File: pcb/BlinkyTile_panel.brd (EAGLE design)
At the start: 220.1 x 170 mm, 220 parts

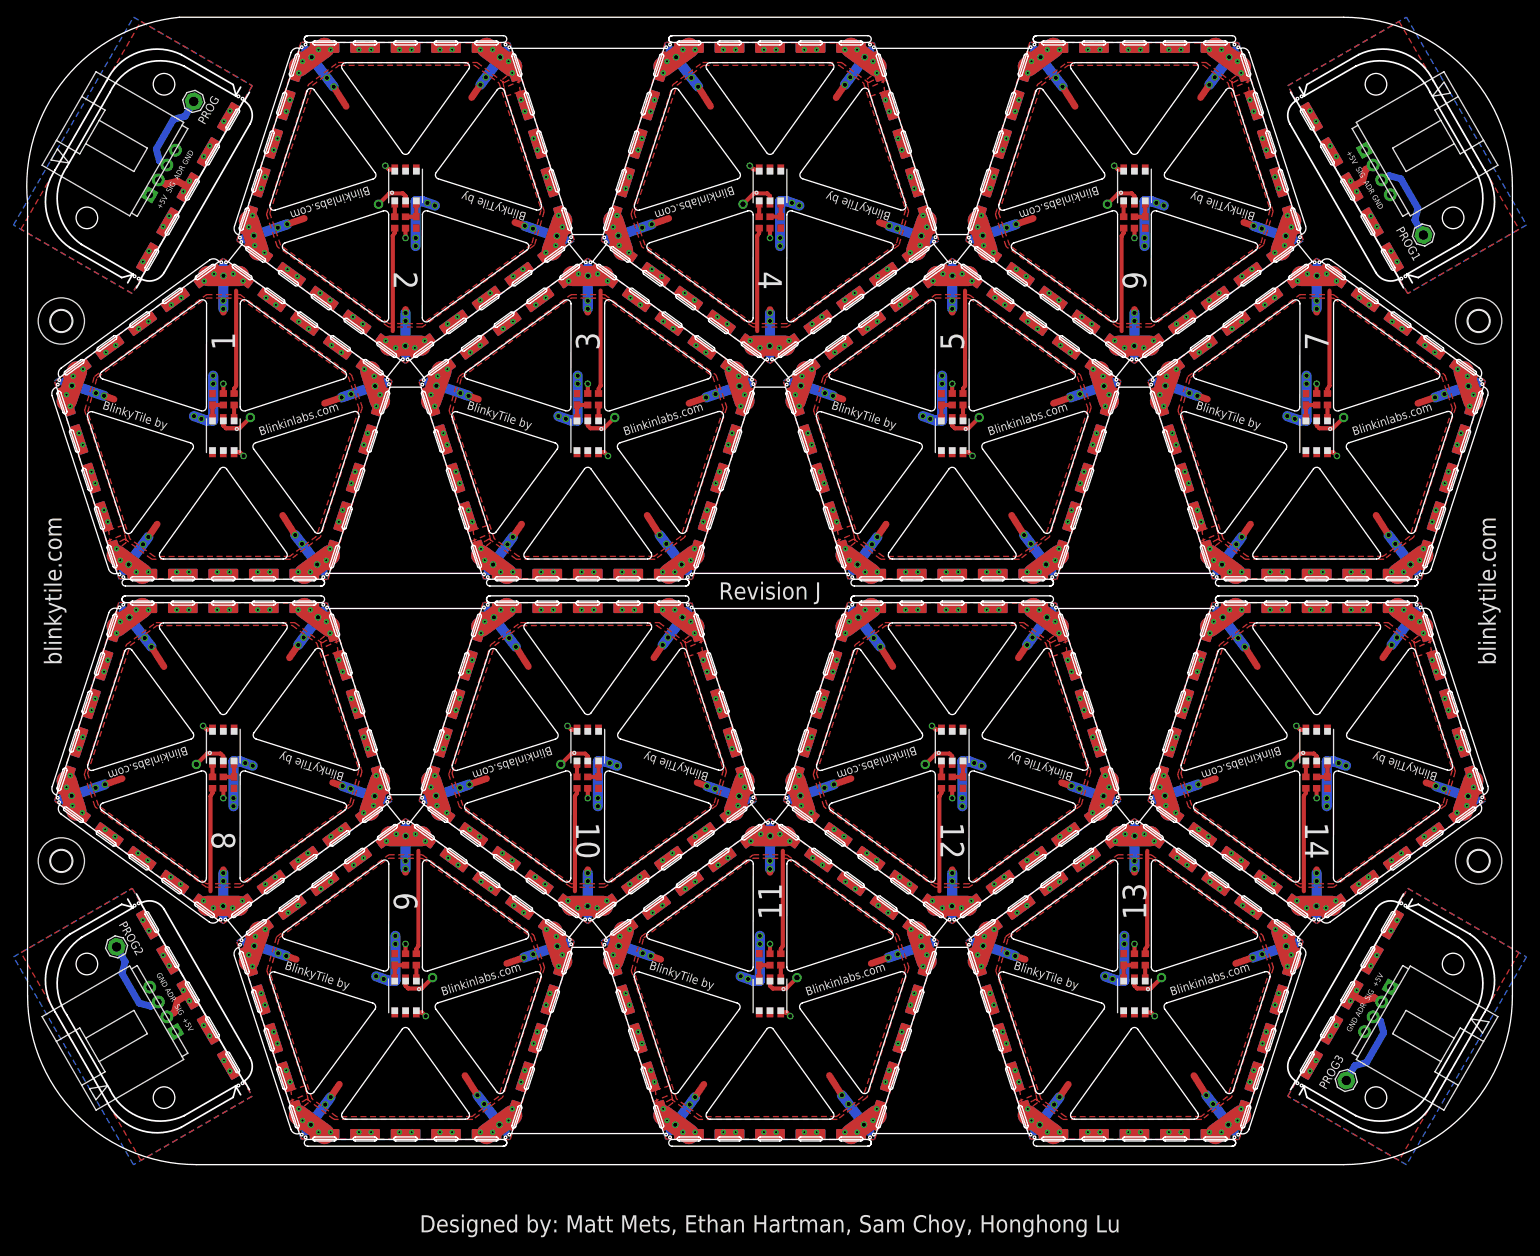
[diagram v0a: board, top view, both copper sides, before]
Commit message: Update panel
- fixed connector board error
- added  fiducial marker at corner
- removed mounting holes at side
- removed 2 connector boards on panel
- added remark for blinkyTile signal
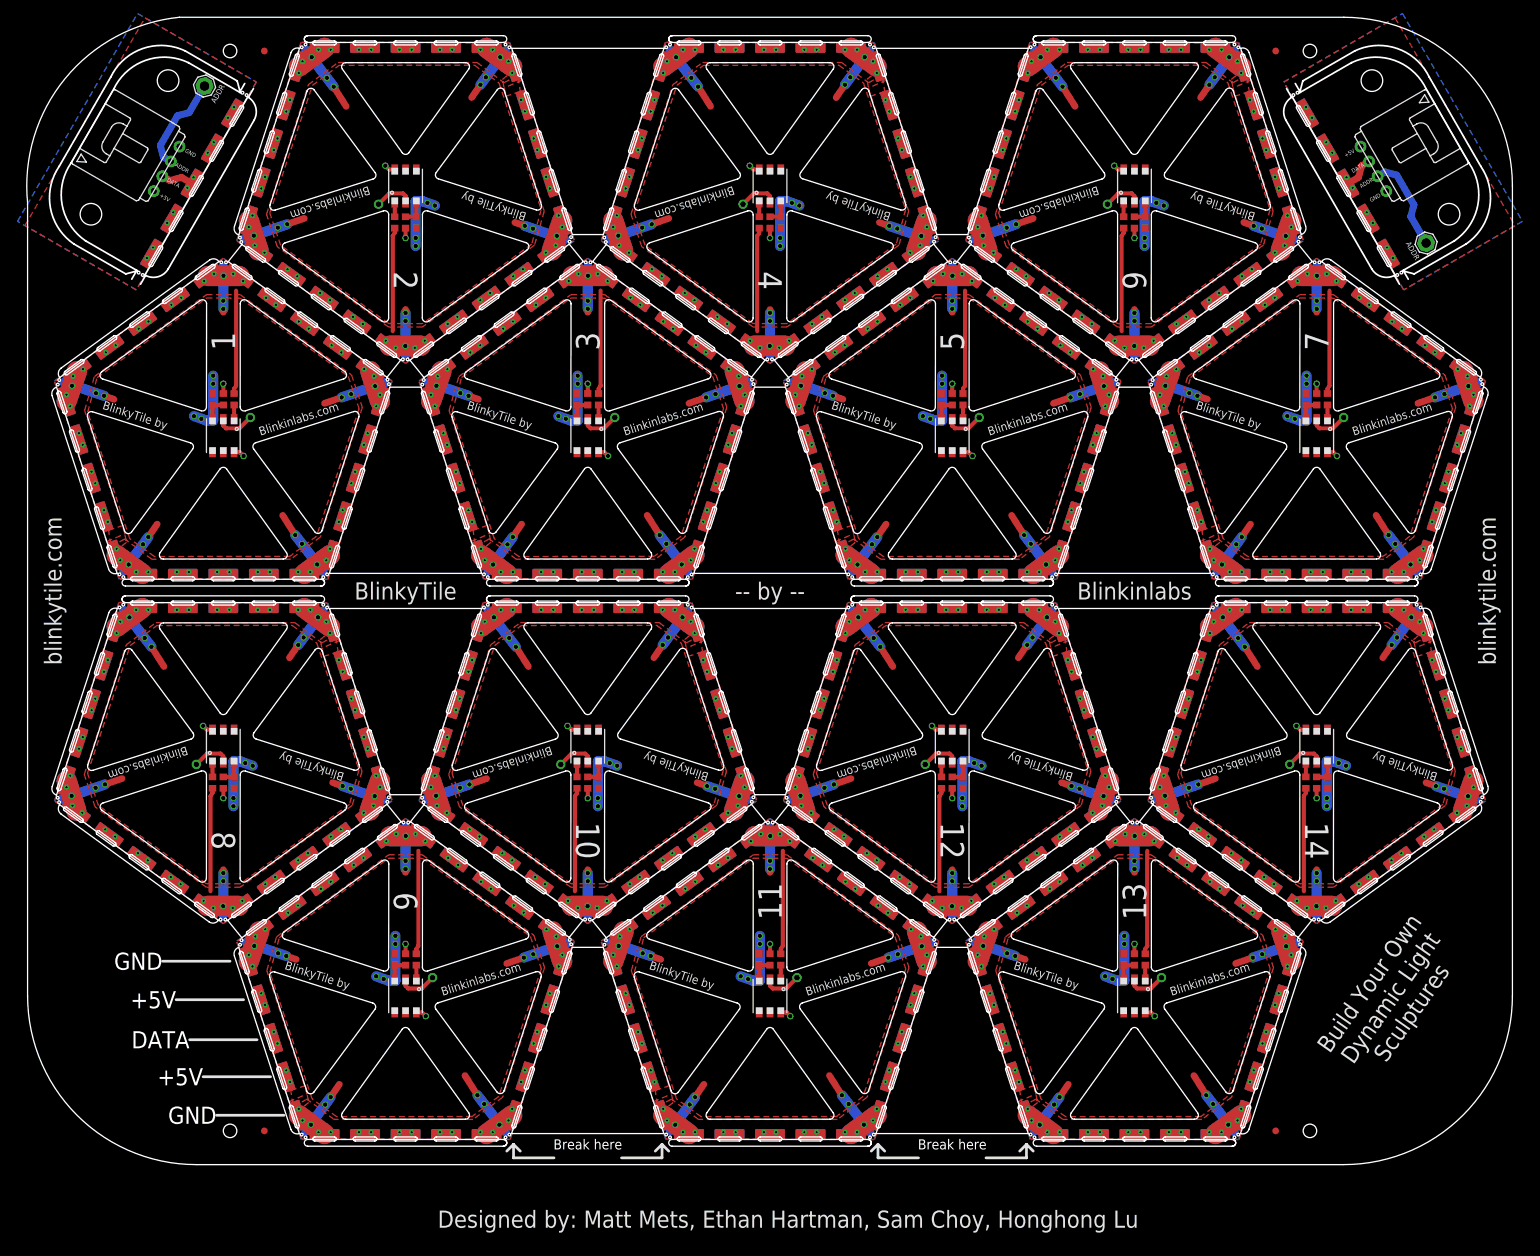
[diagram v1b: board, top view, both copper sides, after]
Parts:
- removed E$81: (no value), dodocohedreled:MOUSE_BITE
- removed E$82: (no value), dodocohedreled:4-PIN_DUPONT
- removed E$91, E$92, E$93, E$94: (no value), holes:3,2
- removed PROG2, PROG3: (no value), solpad:SE14
- removed U$20, U$21: D_EDGEMOD, dodocohedreled:D_EDGE_SLOT_MOD
- E$18, E$76: device dodocohedreled:4-PIN_DUPONT -> Sam-Lib:DUPONT-4P
- E$77, E$78, E$80: device dodocohedreled:MOUSE_BITE -> SparkFun-Aesthetics:FIDUCIAL-1X2
- E$79: device dodocohedreled:4-PIN_DUPONT -> SparkFun-Aesthetics:FIDUCIAL-1X2
- moved E$79 217.6 mm to (74.9, 80.0), turned to 0 degrees
- moved E$78 172.0 mm to (74.9, -80.0), turned to 0 degrees
- moved E$80 172.0 mm to (-74.9, -80.0), turned to 0 degrees
- moved E$77 153.0 mm to (-74.9, 80.0), turned to 0 degrees
- moved PROG 2.78 mm to (-83.8, 74.8)
- moved PROG1 1.26 mm to (97.2, 51.5)
- moved E$16 0.81 mm to (-93.2, 47.1)
- moved E$18 0.81 mm to (-89.4, 62.5)
- moved E$17 0.81 mm to (-77.9, 73.5)
- moved E$20 0.81 mm to (93.2, 47.1)
- moved U$19 0.81 mm to (85.0, 60.0)
- moved U$91 0.81 mm to (-85.0, 60.0)
- moved E$19 0.81 mm to (77.9, 73.5)
- moved E$76 0.81 mm to (89.4, 62.5)
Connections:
- removed net S$11: E$82.P$2, U$21.P$3
- removed net S$12: E$82.P$3, PROG3.MP
- removed net S$6: E$79.P$4, U$20.P$1, U$20.P$5
- removed net S$7: E$79.P$2, U$20.P$3
- removed net S$8: E$79.P$3, PROG2.MP
- removed net S$9: E$82.P$4, U$21.P$1, U$21.P$5
- removed net VCC2: E$79.P$1, U$20.P$7, U$20.P$9
- removed net VCC3: E$82.P$1, U$21.P$7, U$21.P$9
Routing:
- net S$8: track 12.5 -> 0.00 mm
- net S$12: track 12.5 -> 0.00 mm
- net S$7: track 4.88 -> 0.00 mm
- net S$11: track 4.88 -> 0.00 mm
- net S$10: track 12.5 -> 14.5 mm
- net S$5: track 12.5 -> 14.5 mm
- removed copper zone on layer 1, net S$6
- removed copper zone on layer 1, net S$9
- removed copper zone on layer 16, net VCC2
- removed copper zone on layer 16, net VCC3
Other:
- outline, holes or cut-outs redrawn
- board text added: "-- by --"
- board text added: "ADDR"
- board text added: "ADDRESS"
- board text added: "Blinkinlabs"
- board text added: "BlinkyTile"
- board text added: "Break here"
- board text added: "Build Your Own Dynamic Light Sculptures"
- board text added: "DATA"
- board text removed: "ADR"
- board text removed: "Revision J"
- board text removed: "SIG"
